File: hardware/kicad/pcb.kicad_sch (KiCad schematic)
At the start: 6 parts, among them J1 ENCODER, J2 MOTOR, J3 12V MOTOR, U1 Dual_L298N_H_Bridge, U2 Level_Shifter

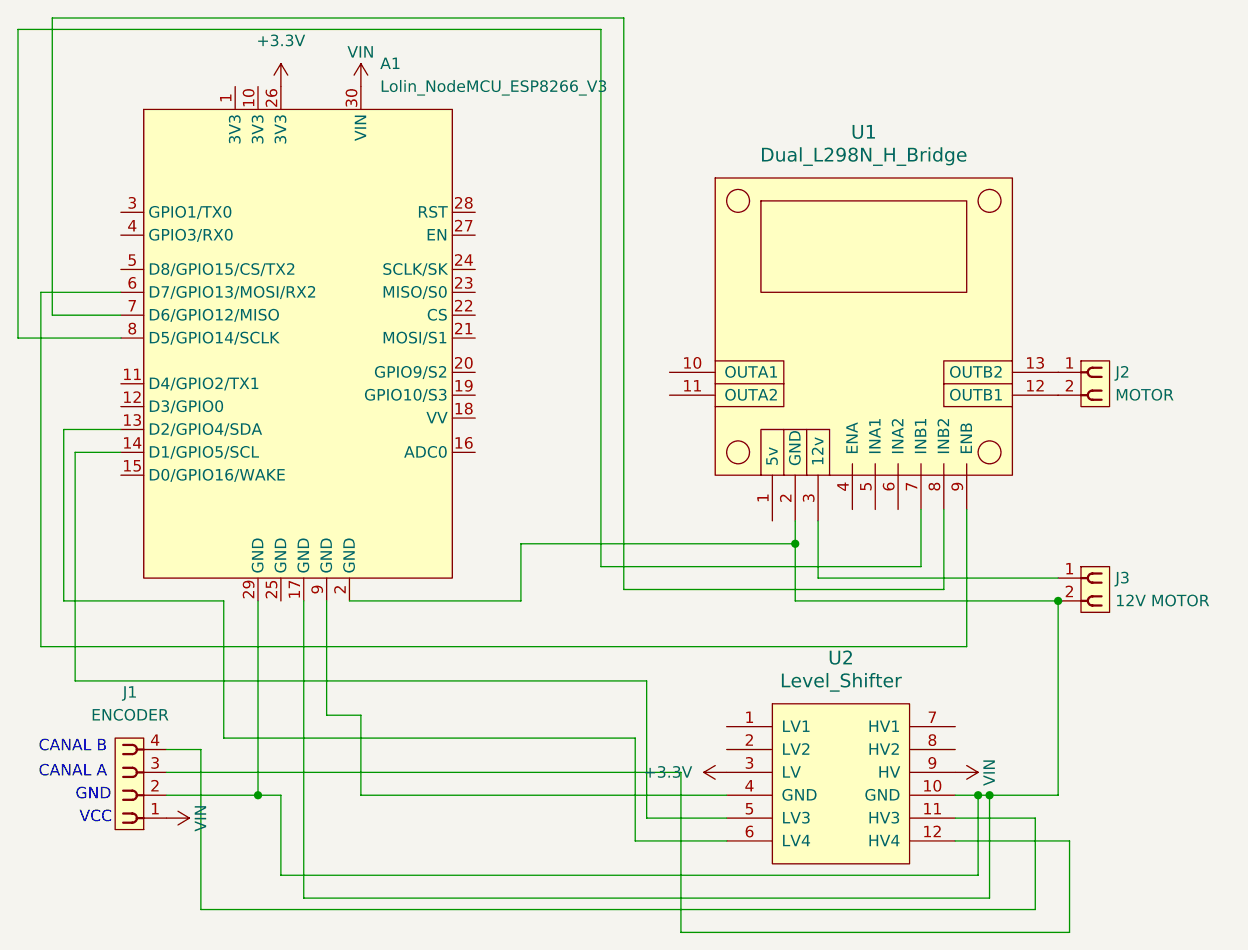
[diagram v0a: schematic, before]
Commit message: fix : corrige erro de orientação nos arquivos gerber
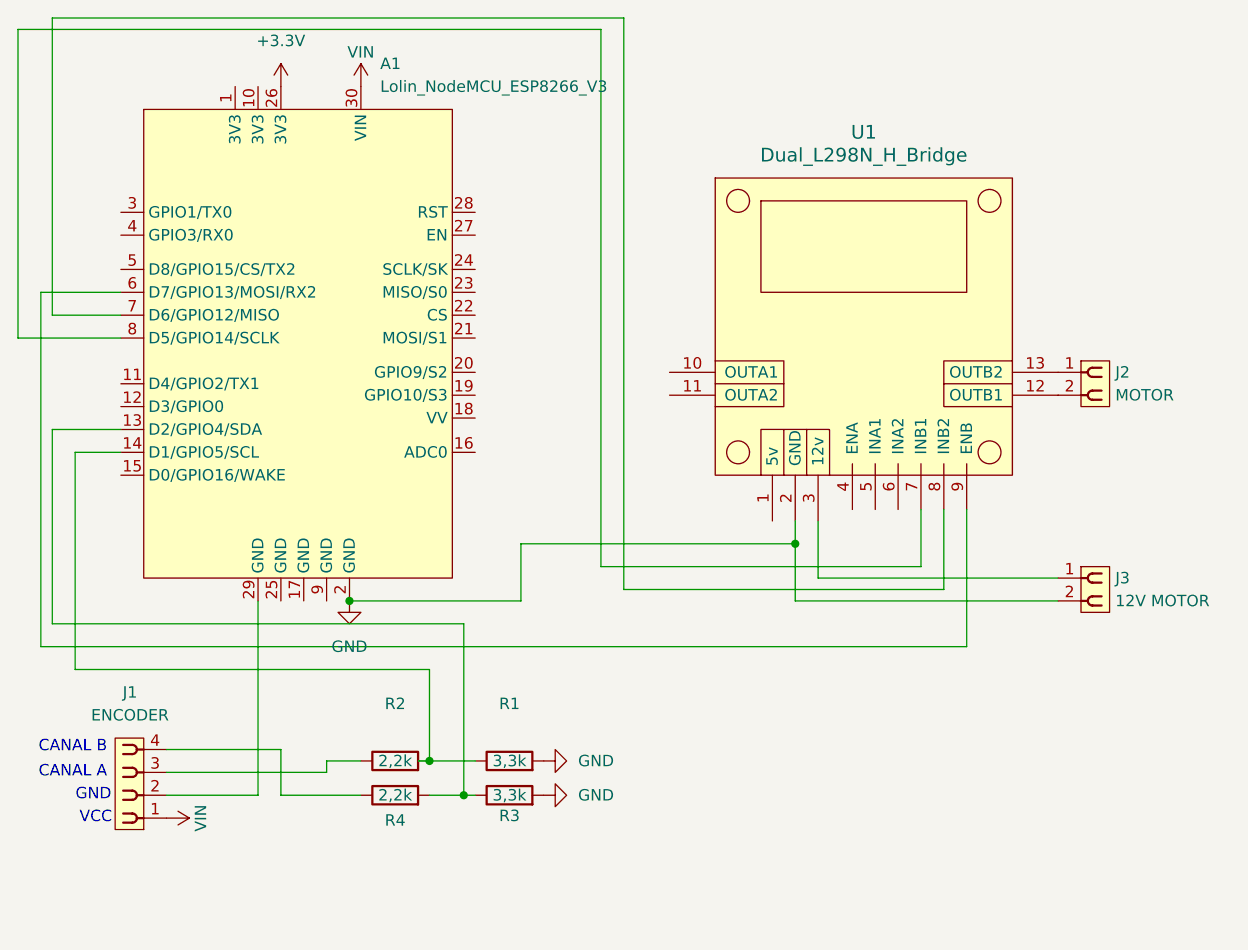
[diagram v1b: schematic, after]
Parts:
- removed U2: Level_Shifter, megasaturnv_custom_components:Level_Shifter, symbol megasaturnv_custom_components:Level_Shifter
- added R1, R3: 3,3k, Resistor_THT:R_Axial_DIN0207_L6.3mm_D2.5mm_P10.16mm_Horizontal, symbol Device:R
- added R2, R4: 2,2k, Resistor_THT:R_Axial_DIN0207_L6.3mm_D2.5mm_P10.16mm_Horizontal, symbol Device:R
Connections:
- net GND: now reaches A1.2 (GND), J3.2, U1.2 (GND)
- net GND: now also R1.2, R3.2; no longer A1.17 (GND), A1.29 (GND), J1.2
- net at J1.3: now also R2.1
- net at J1.4: now also R4.1
- net at A1.14 (D1/GPIO5/SCL): now also R1.1, R2.2
- net at A1.13 (D2/GPIO4/SDA): now also R3.1, R4.2
- new net: A1.29 (GND), J1.2
